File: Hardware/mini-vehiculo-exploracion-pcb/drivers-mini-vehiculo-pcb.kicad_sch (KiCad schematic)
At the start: 25 parts, among them J1 Conn_01x08_Pin_drv, J2 Conn_01x02_Pin_drv, J3 Conn_01x03_Pin, J4 Conn_01x02_Motor1, J5 Conn_01x02_Motor2, U1 DRV8873HPWPRQ1, U2 DRV8873HPWPRQ1

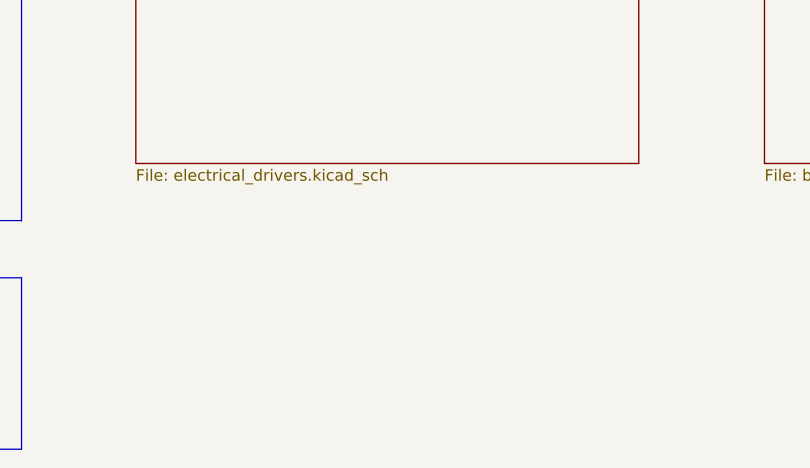
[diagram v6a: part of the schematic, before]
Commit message: adicion de bornera pcb drivers y organizacion de entrada
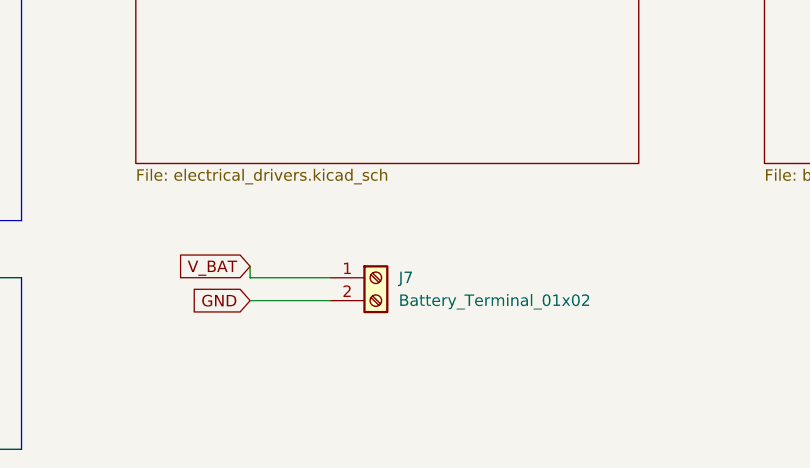
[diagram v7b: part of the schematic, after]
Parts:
- added J7: Battery_Terminal_01x02, TerminalBlock:TerminalBlock_Xinya_XY308-2.54-2P_1x02_P2.54mm_Horizontal, symbol Connector:Screw_Terminal_01x02
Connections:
- net GND: now also J7.2 (Pin_2)
- new net V_BAT: J7.1 (Pin_1)
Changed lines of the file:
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@@
 	(wire
 		(pts
+			(xy 129.54 167.64) (xy 129.54 166.37)
+		)
+		(stroke
+			(width 0)
+			(type default)
+		)
+	)
+	(wire
+		(pts
 			(xy 222.25 96.52) (xy 223.52 96.52)
 		)
@@
 	(wire
 		(pts
+			(xy 129.54 167.64) (xy 138.43 167.64)
+		)
+		(stroke
+			(width 0)
+			(type default)
+		)
+	)
+	(wire
+		(pts
 			(xy 66.04 67.31) (xy 66.04 68.58)
 		)
@@
 	(wire
 		(pts
+			(xy 129.54 170.18) (xy 138.43 170.18)
+		)
+		(stroke
+			(width 0)
+			(type default)
+		)
+	)
+	(wire
+		(pts
 			(xy 60.96 104.14) (xy 60.96 105.41)
 		)
@@
 		)
 	)
+	(global_label "GND"
+		(shape input)
+		(at 129.54 170.18 180)
+		(fields_autoplaced yes)
+		(effects
+			(font
+				(size 1.27 1.27)
+			)
+			(justify right)
+		)
+		(property "Intersheetrefs" "${INTERSHEET_REFS}"
+			(at 122.6843 170.18 0)
+			(effects
+				(font
+					(size 1.27 1.27)
+				)
+				(justify right)
+				(hide yes)
+			)
+		)
+	)
 	(global_label "DVDD_1"
 		(shape input)
@@
 		)
 	)
+	(global_label "V_BAT"
+		(shape input)
+		(at 129.54 166.37 180)
+		(fields_autoplaced yes)
+		(effects
+			(font
+				(size 1.27 1.27)
+			)
+			(justify right)
+		)
+		(property "Intersheetrefs" "${INTERSHEET_REFS}"
+			(at 121.1724 166.37 0)
+			(effects
+				(font
+					(size 1.27 1.27)
+				)
+				(justify right)
+				(hide yes)
+			)
+		)
+	)
 	(symbol
 		(lib_id "power:GND")
@@
 					(unit 1)
 				)
+			)
+		)
+	)
+	(symbol
+		(lib_id "Connector:Screw_Terminal_01x02")
+		(at 143.51 167.64 0)
+		(unit 1)
+		(exclude_from_sim no)
+		(in_bom yes)
+		(on_board yes)
+		(dnp no)
+		(fields_autoplaced yes)
+		(property "Reference" "J7"
+			(at 146.05 167.6399 0)
+			(effects
+				(font
+					(size 1.27 1.27)
+				)
+				(justify left)
+			)
+		)
+		(property "Value" "Battery_Terminal_01x02"
+			(at 146.05 170.1799 0)
+			(effects
+				(font
+					(size 1.27 1.27)
+				)
+				(justify left)
+			)
+		)
+		(property "Footprint" "TerminalBlock:TerminalBlock_Xinya_XY308-2.54-2P_1x02_P2.54mm_Horizontal"
+			(at 143.51 167.64 0)
+			(effects
+				(font
+					(size 1.27 1.27)
+				)
+				(hide yes)
+			)
+		)
+		(property "Datasheet" "~"
+			(at 143.51 167.64 0)
+			(effects
+				(font
+					(size 1.27 1.27)
+				)
+				(hide yes)
+			)
+		)
+		(property "Description" "Generic screw terminal, single row, 01x02, script generated (kicad-library-utils/schlib/autogen/connector/)"
+			(at 143.51 167.64 0)
+			(effects
+				(font
+					(size 1.27 1.27)
+				)
+				(hide yes)
+			)
+		)
+		(pin "1"
+		)
+		(pin "2"
+		)
+		(instances
+			(project "drivers-mini-vehiculo-pcb"
+				(path "/7776e3ee-622a-4a3e-a213-279f6f5df2cb"
+					(reference "J7")
+					(unit 1)
+				)
